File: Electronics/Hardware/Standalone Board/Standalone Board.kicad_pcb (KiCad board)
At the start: 4 copper layers, 163.8 x 63.5 mm, 146 parts, among them J1 2309411-2, J10 PWR_IN, J11 FH35C-39S-0.3SHW(50) Left, J12 FH35C-39S-0.3SHW(50) Right, J2 USB_A, J3 GPIO, J4 DBG_UART1, J5 FAN1, J6 2041119-1, J7 2290741-1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

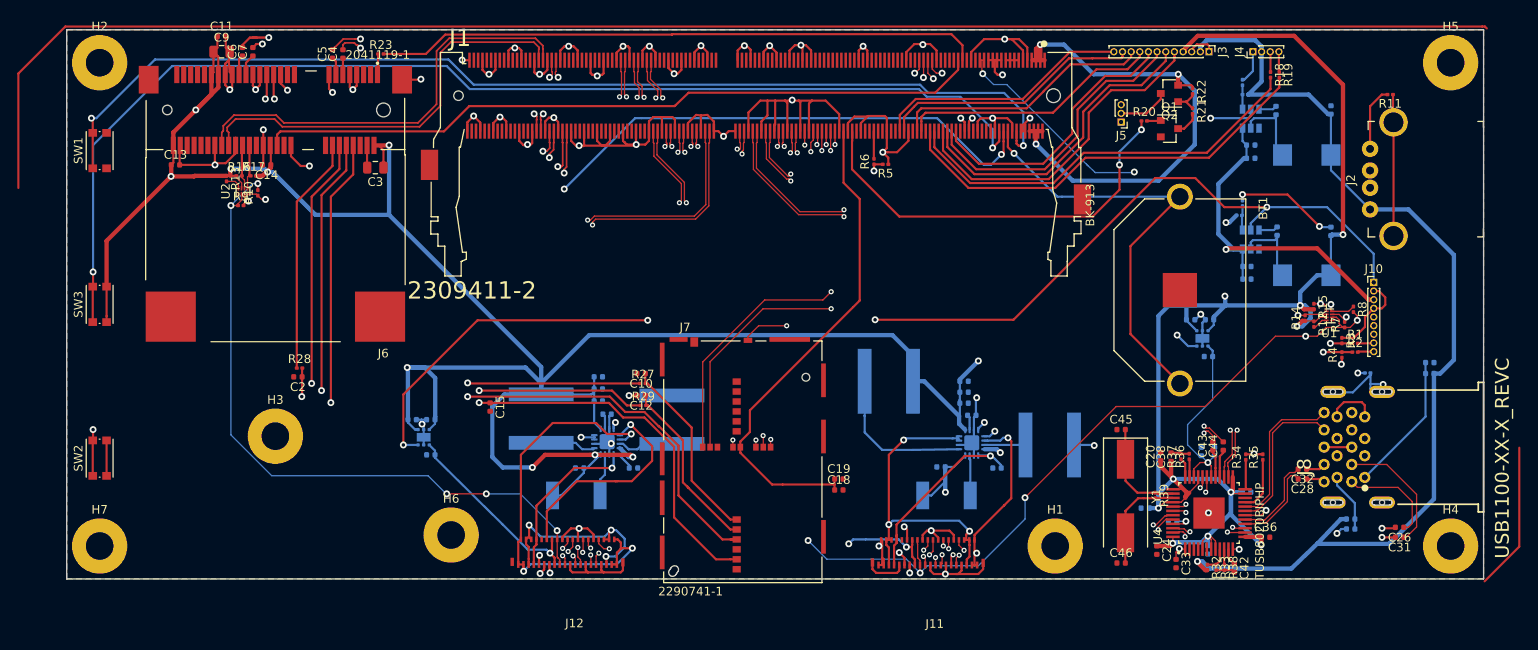
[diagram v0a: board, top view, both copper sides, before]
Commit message: Fix silkscreen
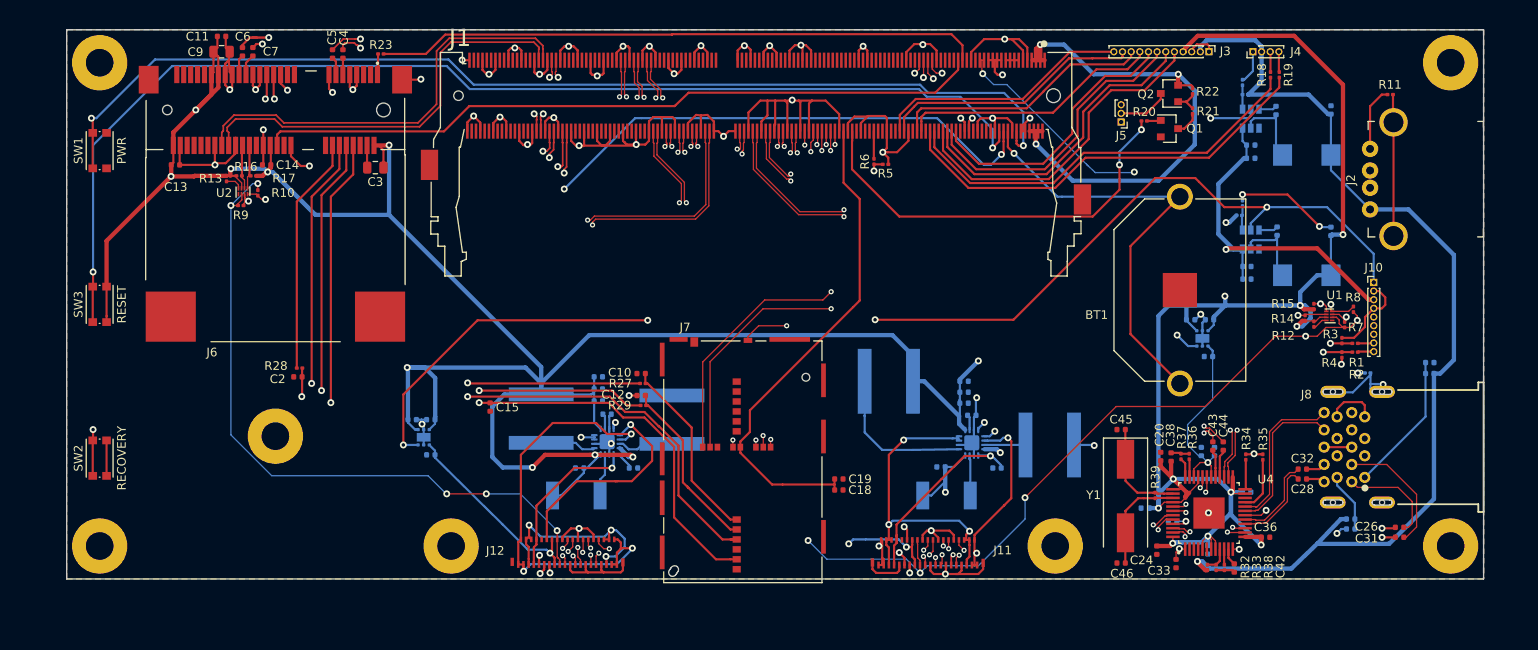
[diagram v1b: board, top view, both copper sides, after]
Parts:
- moved H6 1.27 mm to (95.2, 110.5)
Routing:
- net (no net): track 202.5 -> 0.00 mm
